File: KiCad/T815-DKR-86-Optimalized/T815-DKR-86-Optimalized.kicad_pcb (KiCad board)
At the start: 2 copper layers, 42 parts, among them J1 PWM Steering, J2 PWM Throttle, J3 PWM 3.ch.button, M1 RC Model Motor, Q1 BS170, Q3 BS170, Q4 BS170, Q6 BS170, Q7 BS170, U4 PWM_MOSFET_Module

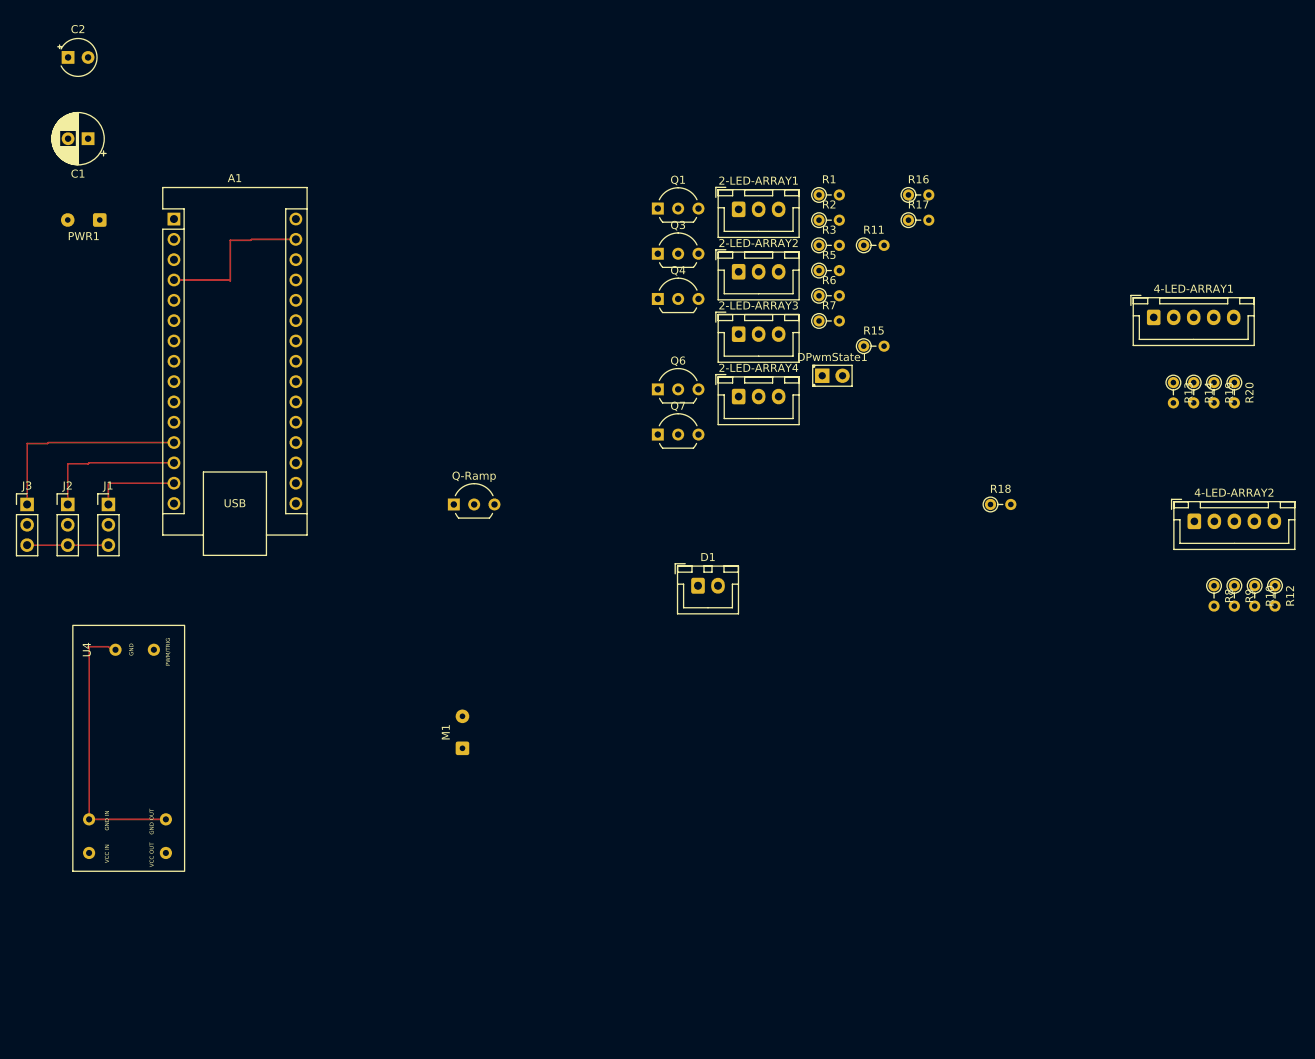
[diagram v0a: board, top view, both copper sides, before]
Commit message: schema update - rearanged pins.
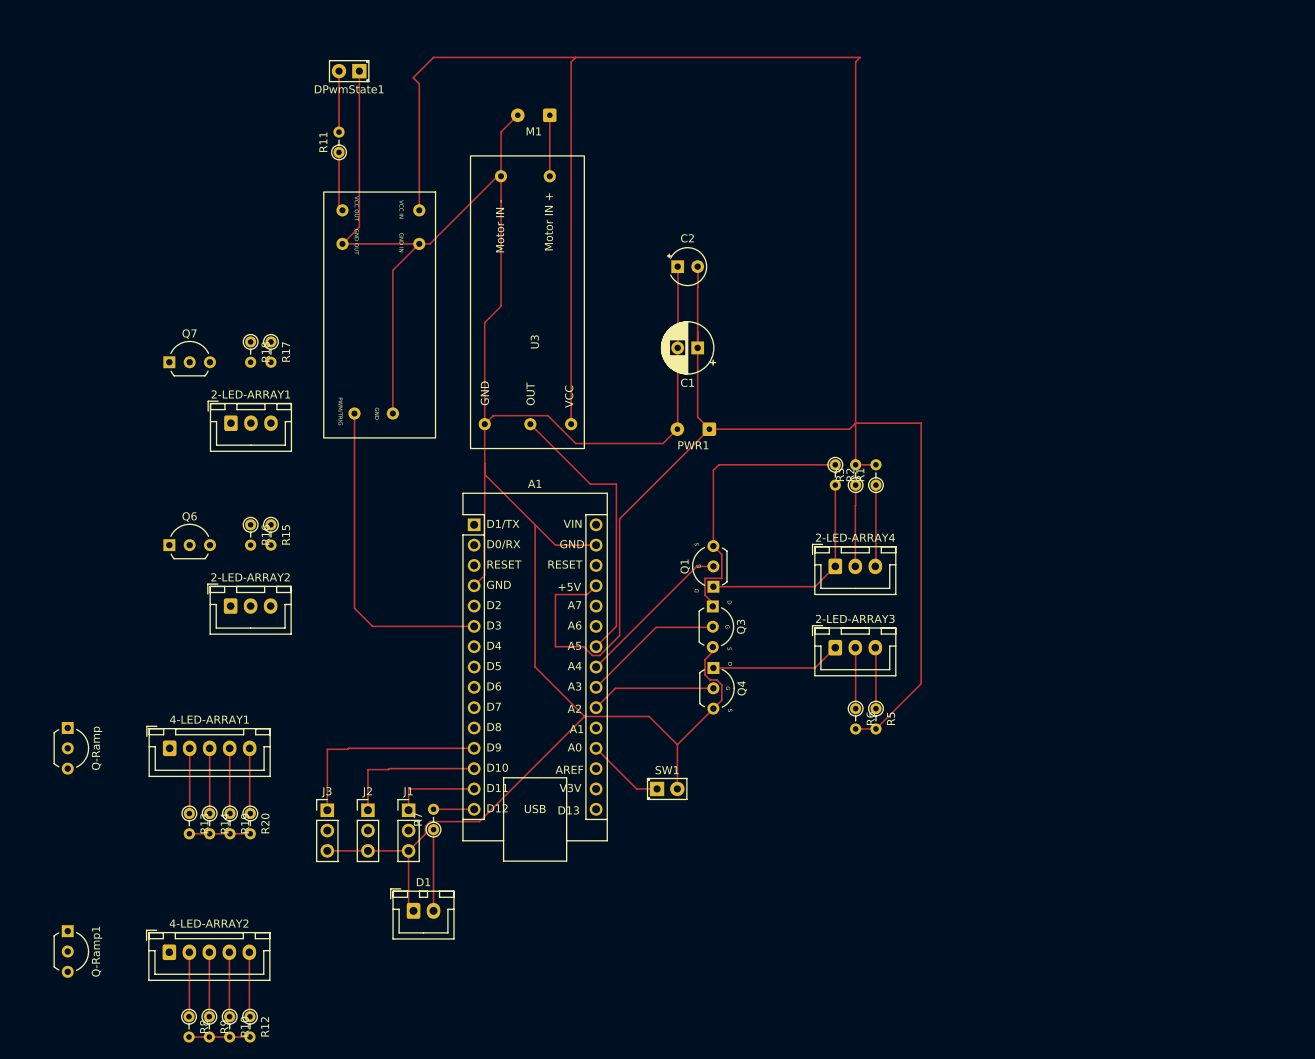
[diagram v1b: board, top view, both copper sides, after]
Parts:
- added Q-Ramp1: BS170, Package_TO_SOT_THT:TO-92L_Inline_Wide, F.Cu at (22.9, 129.5)
- added SW1: SW_Calibration, LED_THT:LED_D2.0mm_W4.8mm_H2.5mm_FlatTop, F.Cu at (96.5, 111.8)
- added U3: Optocoupler_Module, FootPrintProjectLibrary:Izolační modul s optočlenem, F.Cu at (75.0, 66.2)
- A1: footprint Module:Arduino_Nano -> FootPrintProjectLibrary:Arduino_Nano
- Q1, Q3, Q4: footprint Package_TO_SOT_THT:TO-92L_Inline_Wide -> FootPrintProjectLibrary:BS170-TO-92L_Inline_Wide
- moved R10 139.0 mm to (43.1, 140.2)
- moved R12 139.0 mm to (45.6, 140.2)
- moved 4-LED-ARRAY2 139.0 mm to (35.6, 132.2)
- moved R8 139.0 mm to (38.0, 140.2)
- moved R9 139.0 mm to (40.6, 140.2)
- moved 4-LED-ARRAY1 134.3 mm to (35.6, 106.7)
- moved R14 134.3 mm to (40.6, 114.8)
- moved R19 134.3 mm to (43.1, 114.8)
- moved R13 134.3 mm to (38.1, 114.8)
- moved R20 134.3 mm to (45.7, 114.8)
- moved R18 94.7 mm to (45.7, 55.9), turned to -90 degrees
- moved R16 92.0 mm to (45.7, 78.7), turned to -90 degrees
- moved U4 90.3 mm to (66.8, 39.4), turned to -90 degrees
- moved R17 81.1 mm to (48.3, 55.9), turned to -90 degrees
- moved PWR1 80.6 mm to (103.1, 66.8)
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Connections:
- A1 pad 10: Net-(A1-D7) -> unconnected-(A1-D7-Pad10)
- A1 pad 11: Net-(A1-D8) -> unconnected-(A1-D8-Pad11)
- A1 pad 19: unconnected-(A1-A0-Pad19) -> Net-(A1-A0)
- A1 pad 20: Net-(A1-A1) -> unconnected-(A1-A1-Pad20)
- A1 pad 23: unconnected-(A1-A4-Pad23) -> Net-(A1-A4)
- A1 pad 24: unconnected-(A1-A5-Pad24) -> Net-(A1-A5)
- Q1 pad 1: Net-(A1-A3) -> Net-(A1-A4)
- Q3 pad 1: Net-(A1-A2) -> Net-(A1-A3)
- Q4 pad 1: Net-(A1-D8) -> Net-(A1-A2)
- Q6 pad 1: Net-(A1-D7) -> unconnected-(A1-D7-Pad10)
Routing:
- net Net-(A1-+5V): track 0.00 -> 318.5 mm
- net GND: track 65.4 -> 304.2 mm
- net Net-(A1-D3): track 0.00 -> 40.2 mm
- net Net-(Q1-S): track 0.00 -> 36.1 mm
- net Net-(A1-A5): track 0.00 -> 35.2 mm
- net Net-(2-LED-ARRAY4-GND): track 0.00 -> 26.5 mm
- net /PWM 5V branch: track 0.00 -> 22.7 mm
- net Net-(A1-A4): track 0.00 -> 19.9 mm
- net Net-(A1-A3): track 0.00 -> 17.8 mm
- net Net-(2-LED-ARRAY3-GND): track 0.00 -> 16.3 mm
- net Net-(A1-A2): track 0.00 -> 15.7 mm
- net Net-(2-LED-ARRAY4-LED2): track 0.00 -> 10.2 mm
- net Net-(2-LED-ARRAY4-LED1): track 0.00 -> 10.2 mm
- net Net-(D1-A): track 0.00 -> 10.2 mm
- net Net-(A1-A0): track 0.00 -> 9.72 mm
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
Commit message: schema update - pcb more optima use of arduino pins
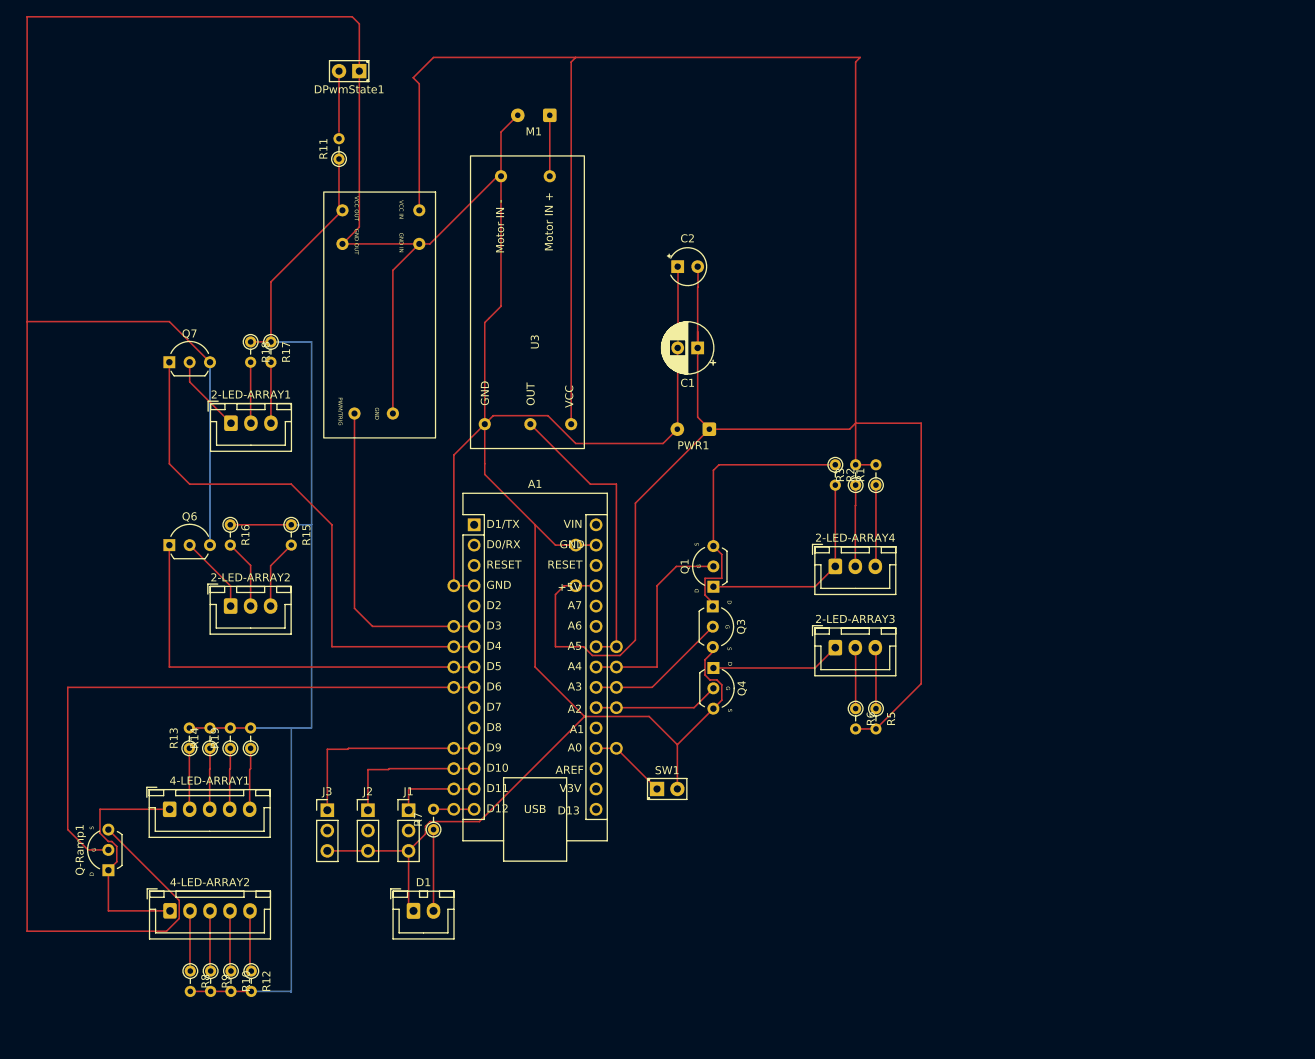
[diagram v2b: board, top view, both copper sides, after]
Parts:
- removed Q-Ramp: BS170, Package_TO_SOT_THT:TO-92L_Inline_Wide
- added ?: , , F.Cu at (71.1, 96.5)
- added ?: , , F.Cu at (71.1, 94.0)
- added ?: , , F.Cu at (91.4, 101.6)
- added ?: , , F.Cu at (71.1, 99.1)
- added ?: , , F.Cu at (71.1, 86.4)
- added ?: , , F.Cu at (86.4, 81.3)
- added ?: , , F.Cu at (71.1, 91.4)
- added ?: , , F.Cu at (71.1, 111.8)
- added ?: , , F.Cu at (91.4, 96.5)
- added ?: , , F.Cu at (91.4, 106.7)
- added ?: , , F.Cu at (71.1, 106.7)
- added ?: , , F.Cu at (91.4, 99.1)
- added ?: , , F.Cu at (91.4, 94.0)
- added ?: , , F.Cu at (71.1, 109.2)
- added ?: , , F.Cu at (71.1, 114.3)
- added ?: , , F.Cu at (86.4, 86.4)
- Q-Ramp1: footprint Package_TO_SOT_THT:TO-92L_Inline_Wide -> FootPrintProjectLibrary:BS170-TO-92L_Inline_Wide
- moved Q-Ramp1 9.16 mm to (27.9, 121.9), turned to 90 degrees
- moved R14 8.15 mm to (40.6, 106.7), turned to 90 degrees
- moved R19 8.15 mm to (43.2, 106.7), turned to 90 degrees
- moved R20 8.15 mm to (45.7, 106.7), turned to 90 degrees
- moved R13 8.14 mm to (38.1, 106.7), turned to 90 degrees
- moved 4-LED-ARRAY1 7.62 mm to (35.6, 114.3)
- moved R10 5.70 mm to (43.3, 134.5)
- moved R12 5.70 mm to (45.8, 134.5)
- moved R8 5.70 mm to (38.2, 134.5)
- moved R9 5.70 mm to (40.7, 134.5)
- moved 4-LED-ARRAY2 5.18 mm to (35.6, 127.0)
- moved R15 2.54 mm to (50.8, 78.7)
- moved R16 2.54 mm to (43.2, 78.7)
- moved R11 0.83 mm to (56.8, 33.0)
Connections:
- A1 pad 5: Net-(A1-D2) -> unconnected-(A1-D2-Pad5)
- A1 pad 8: unconnected-(A1-D5-Pad8) -> Net-(A1-D5)
- A1 pad 9: unconnected-(A1-D6-Pad9) -> Net-(A1-D6)
- Q-Ramp1 pad 1: Net-(A1-D2) -> Net-(A1-D6)
- Q6 pad 1: unconnected-(A1-D7-Pad10) -> Net-(A1-D5)
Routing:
- net GND: track 304.2 -> 557.1 mm
- net /PWM 5V branch: track 22.7 -> 154.6 mm
- net Net-(A1-D6): track 0.00 -> 74.7 mm
- net Net-(A1-D4): track 0.00 -> 69.2 mm
- net Net-(A1-D5): track 0.00 -> 53.3 mm
- net Net-(4-LED-ARRAY1-GND): track 0.00 -> 30.7 mm
- net Net-(2-LED-ARRAY1-GND): track 0.00 -> 9.76 mm
- net Net-(2-LED-ARRAY2-GND): track 0.00 -> 9.74 mm
- net Net-(2-LED-ARRAY2-LED2): track 0.00 -> 8.69 mm
- net Net-(2-LED-ARRAY2-LED1): track 0.00 -> 8.67 mm
- net Net-(2-LED-ARRAY1-LED1): track 0.00 -> 7.64 mm
- net Net-(2-LED-ARRAY1-LED2): track 0.00 -> 7.62 mm
- net Net-(A1-A4): track 19.9 -> 25.8 mm
- net Net-(A1-A5): track 35.2 -> 36.7 mm
- net Net-(A1-+5V): track 318.5 -> 320.0 mm
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
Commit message: none
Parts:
- removed 2-LED-ARRAY1, 2-LED-ARRAY2, 2-LED-ARRAY3, 2-LED-ARRAY4: ~, Connector_JST:JST_XH_B3B-XH-A_1x03_P2.50mm_Vertical
- removed 4-LED-ARRAY1, 4-LED-ARRAY2: ~, Connector_JST:JST_XH_B5B-XH-A_1x05_P2.50mm_Vertical
- added 2-LED-ARRAY-INNER-BREAKS1: ~, Connector_JST:JST_XH_B3B-XH-A_1x03_P2.50mm_Vertical, F.Cu at (118.9, 96.5)
- added 2-LED-ARRAY-INNER-FRONT1: ~, Connector_JST:JST_XH_B3B-XH-A_1x03_P2.50mm_Vertical, F.Cu at (43.3, 66.0)
- added 2-LED-ARRAY-OUTER-BREAKS1: ~, Connector_JST:JST_XH_B3B-XH-A_1x03_P2.50mm_Vertical, F.Cu at (118.8, 86.3)
- added 2-LED-ARRAY-OUTER-FRONT1: ~, Connector_JST:JST_XH_B3B-XH-A_1x03_P2.50mm_Vertical, F.Cu at (43.3, 88.9)
- added 4-LED-ARRAY-RAMP1: ~, Connector_JST:JST_XH_B5B-XH-A_1x05_P2.50mm_Vertical, F.Cu at (35.6, 114.3)
- added 4-LED-ARRAY-RAMP2: ~, Connector_JST:JST_XH_B5B-XH-A_1x05_P2.50mm_Vertical, F.Cu at (35.7, 127.0)
- D1: value White Reverse -> LED-REVERSE
- DPwmState1: value Optional PWM state LED -> PWM-STATE-LED
- moved J3 13.2 mm to (66.0, 106.7), turned to -90 degrees
- moved D1 9.16 mm to (61.0, 119.4)
- moved J2 7.68 mm to (66.0, 109.2), turned to -90 degrees
- moved R7 3.59 mm to (66.0, 114.3), turned to 0 degrees
- moved J1 2.72 mm to (66.0, 111.8), turned to -90 degrees
- moved R1 2.42 mm to (123.9, 76.2)
- moved R2 2.42 mm to (118.8, 73.7)
- moved R3 2.42 mm to (121.3, 76.2)
- moved R5 2.42 mm to (123.9, 104.1)
- moved R6 2.42 mm to (121.3, 104.1)
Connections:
- R11 pad 1: /PWM 5V branch -> Net-(JP1-A)
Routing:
- net Net-(A1-D9): track 26.0 -> 7.62 mm
- net Net-(A1-D10): track 18.4 -> 7.62 mm
- net Net-(D1-A): track 10.2 -> 6.13 mm
- net Net-(A1-D11): track 10.8 -> 7.62 mm
- net Net-(A1-+5V): track 320.0 -> 322.3 mm
- net Net-(Q1-S): track 36.1 -> 34.1 mm
- net Net-(2-LED-ARRAY-OUTER-BREAKS1-GND): track 26.5 -> 25.4 mm
- net Net-(2-LED-ARRAY-INNER-BREAKS1-GND): track 16.3 -> 15.3 mm
- net GND: track 557.1 -> 558.1 mm
